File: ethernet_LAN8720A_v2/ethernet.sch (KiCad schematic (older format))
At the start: 46 parts, among them P1 SI-52003-F, P3 PoE, U1 LAN8720A-CP, U2 ASV-50.000MHZ-E-T

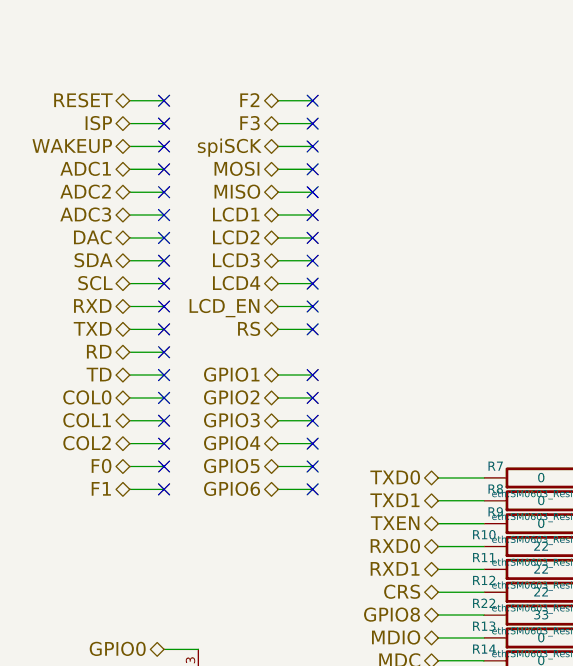
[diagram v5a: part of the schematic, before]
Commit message: Modifico el Poncho ETH para que sea solo Poncho Izquierdo.
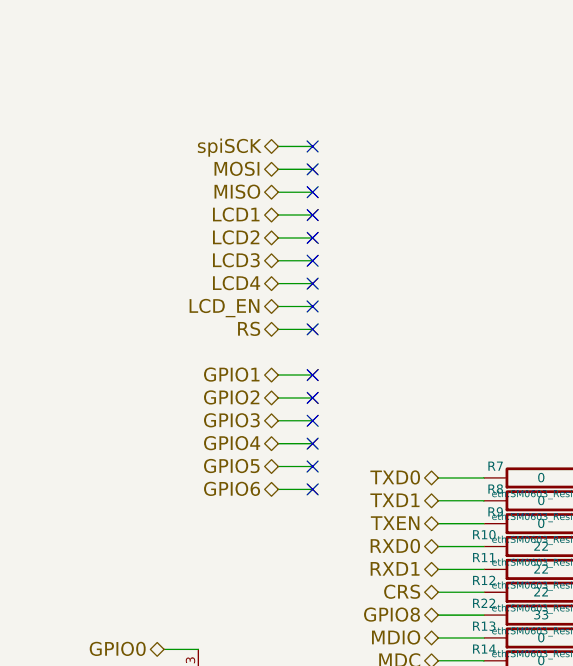
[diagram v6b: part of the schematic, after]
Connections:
- no-connect marks 37 -> 17
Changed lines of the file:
@@
 	0    -1   -1   0
 $EndComp
-Text HLabel 1000 950  0    60   BiDi ~ 0
-RESET
-Text HLabel 1000 1050 0    60   BiDi ~ 0
-ISP
-Text HLabel 1000 1150 0    60   BiDi ~ 0
-WAKEUP
-Text HLabel 1000 1250 0    60   BiDi ~ 0
-ADC1
-Text HLabel 1000 1350 0    60   BiDi ~ 0
-ADC2
-Text HLabel 1000 1450 0    60   BiDi ~ 0
-ADC3
-Text HLabel 1000 1550 0    60   BiDi ~ 0
-DAC
-Text HLabel 1000 1650 0    60   BiDi ~ 0
-SDA
-Text HLabel 1000 1750 0    60   BiDi ~ 0
-SCL
-Text HLabel 1000 1850 0    60   BiDi ~ 0
-RXD
-Text HLabel 1000 1950 0    60   BiDi ~ 0
-TXD
-Text HLabel 1000 2050 0    60   BiDi ~ 0
-RD
-Text HLabel 1000 2150 0    60   BiDi ~ 0
-TD
-Text HLabel 1000 2250 0    60   BiDi ~ 0
-COL0
-Text HLabel 1000 2350 0    60   BiDi ~ 0
-COL1
-Text HLabel 1000 2450 0    60   BiDi ~ 0
-COL2
-Text HLabel 1000 2550 0    60   BiDi ~ 0
-F0
-Text HLabel 1000 2650 0    60   BiDi ~ 0
-F1
-Text HLabel 1650 950  0    60   BiDi ~ 0
-F2
-Text HLabel 1650 1050 0    60   BiDi ~ 0
-F3
 Text HLabel 1650 1150 0    60   BiDi ~ 0
 spiSCK
@@
 Text HLabel 1650 1450 0    60   BiDi ~ 0
 LCD1
-NoConn ~ 1150 950
-NoConn ~ 1150 1050
-NoConn ~ 1150 1150
-NoConn ~ 1150 1250
-NoConn ~ 1150 1350
-NoConn ~ 1150 1450
-NoConn ~ 1150 1550
-NoConn ~ 1150 1650
-NoConn ~ 1150 1750
-NoConn ~ 1150 1850
-NoConn ~ 1150 1950
-NoConn ~ 1150 2050
-NoConn ~ 1150 2150
-NoConn ~ 1150 2250
-NoConn ~ 1150 2350
-NoConn ~ 1150 2450
-NoConn ~ 1150 2550
-NoConn ~ 1150 2650
-NoConn ~ 1800 950
-NoConn ~ 1800 1050
 NoConn ~ 1800 1150
 NoConn ~ 1800 1250
@@
 Text HLabel 1650 1750 0    60   BiDi ~ 0
 LCD4
-Text HLabel 1650 1850 0    60   BiDi ~ 0
-LCD_EN
 Text HLabel 1650 1950 0    60   BiDi ~ 0
 RS
@@
 	3050 3200 3950 3200
 Wire Wire Line
-	1150 950  1000 950
-Wire Wire Line
-	1000 1050 1150 1050
-Wire Wire Line
-	1000 1150 1150 1150
-Wire Wire Line
-	1000 1250 1150 1250
-Wire Wire Line
-	1000 1350 1150 1350
-Wire Wire Line
-	1000 1450 1150 1450
-Wire Wire Line
-	1000 1550 1150 1550
-Wire Wire Line
-	1000 1650 1150 1650
-Wire Wire Line
-	1150 1750 1000 1750
-Wire Wire Line
-	1000 1850 1150 1850
-Wire Wire Line
-	1000 1950 1150 1950
-Wire Wire Line
-	1000 2050 1150 2050
-Wire Wire Line
-	1000 2150 1150 2150
-Wire Wire Line
-	1000 2250 1150 2250
-Wire Wire Line
-	1000 2350 1150 2350
-Wire Wire Line
-	1000 2450 1150 2450
-Wire Wire Line
-	1150 2550 1000 2550
-Wire Wire Line
-	1000 2650 1150 2650
-Wire Wire Line
-	1650 950  1800 950
-Wire Wire Line
-	1650 1050 1800 1050
-Wire Wire Line
 	1650 1150 1800 1150
 Wire Wire Line
@@
 Text Label 7750 3000 0    60   ~ 0
 Rx_N
+Text HLabel 1650 1850 0    60   BiDi ~ 0
+LCD_EN
 $EndSCHEMATC
